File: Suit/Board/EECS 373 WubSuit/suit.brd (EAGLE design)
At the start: 100 x 80 mm, 44 parts, among them U1 ATMEGA328P_PDIP

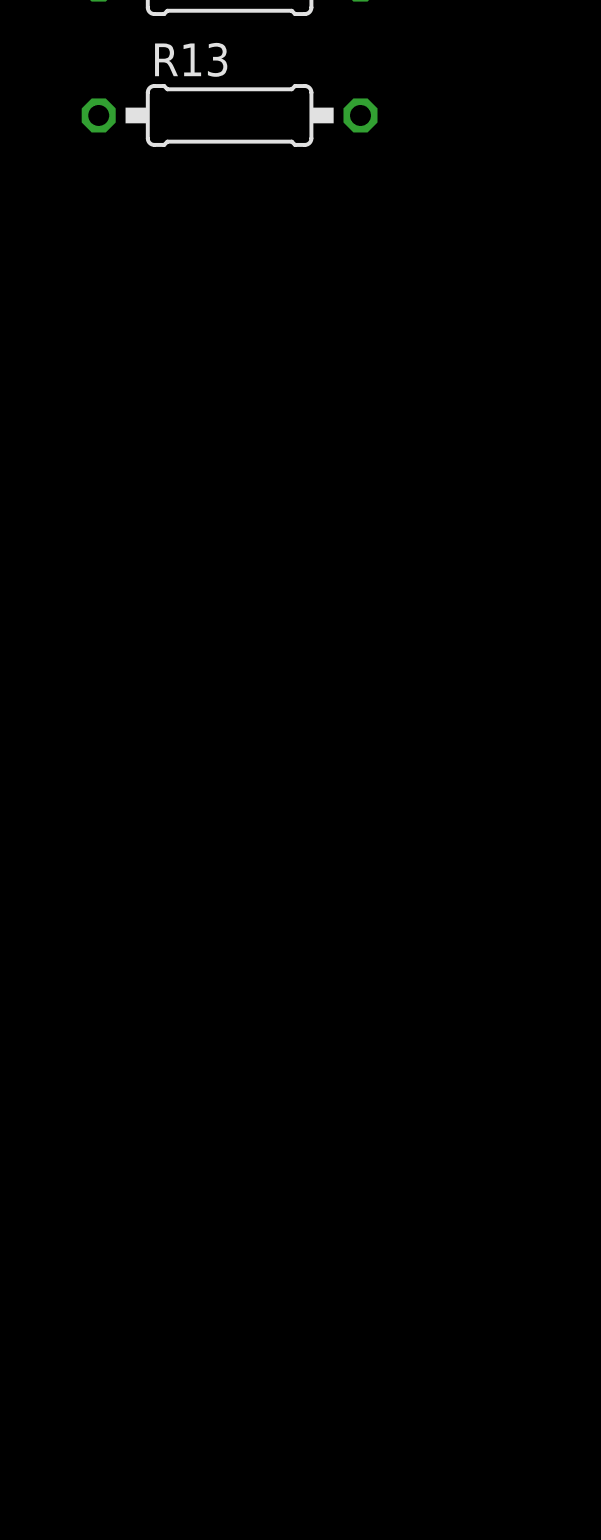
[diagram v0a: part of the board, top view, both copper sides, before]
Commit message: added more board/sch files
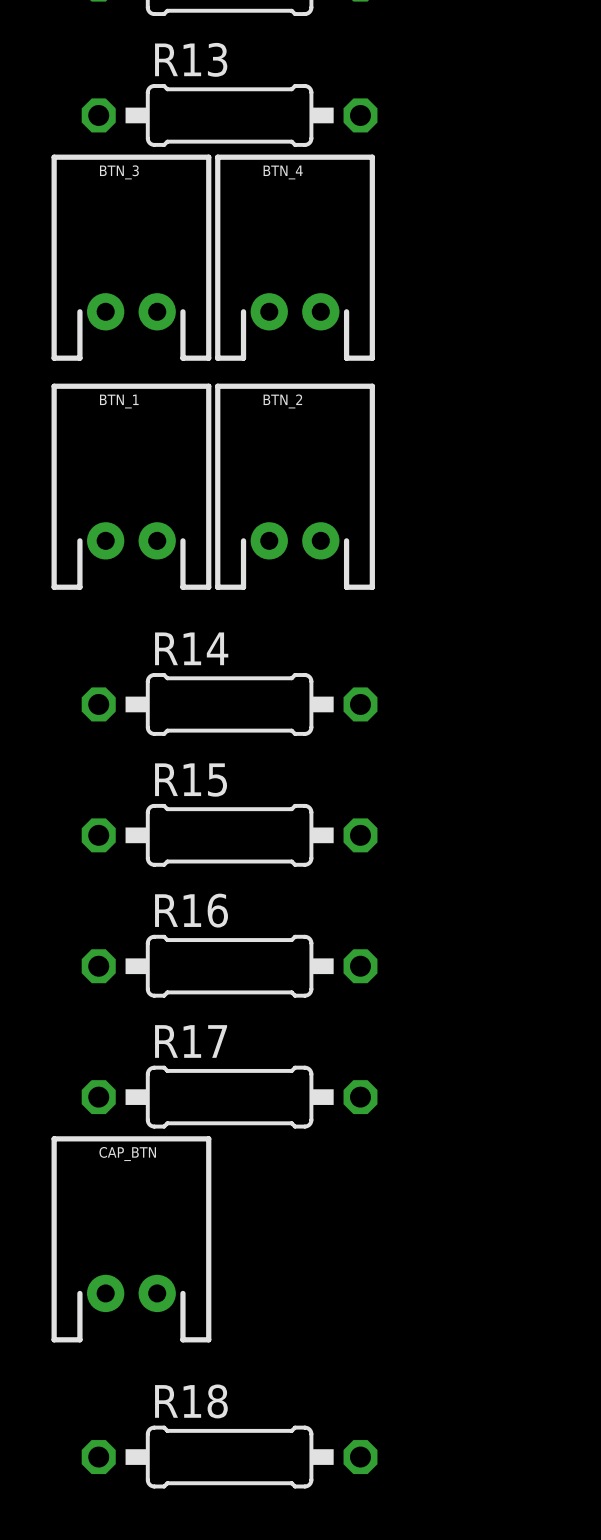
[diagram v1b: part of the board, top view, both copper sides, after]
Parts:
- added BTN_1, BTN_2, BTN_3, BTN_4, CAP_BTN: M02JST-PTH-2, SparkFun-Connectors:JST-2-PTH
- added R14, R15, R16, R17, R18: 10k, resistor:0207/10
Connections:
- new net BTN_1: BTN_1.1, R17.1, XB1.17
- new net BTN_2: BTN_2.1, R16.1, XB1.11
- new net BTN_3: BTN_3.1, R15.1, XB1.15
- new net BTN_4: BTN_4.1, R14.1, XB1.16
- net CAP_BTN: now also CAP_BTN.1, R18.1
- net GND: now also MMA8452.1, R14.2, R15.2, R16.2, R17.2, R18.2
- net RST: now also XB1.5
- net SCL: now also MMA8452.4
- net SDA: now also MMA8452.5
- net VCC: now also BTN_1.2, BTN_2.2, BTN_3.2, BTN_4.2, CAP_BTN.2, MMA8452.6
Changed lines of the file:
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@@
 <element name="R12" library="resistor" package="0207/10" value="1M" x="-152.4" y="-267.97"/>
 <element name="R13" library="resistor" package="0207/10" value="1M" x="-152.4" y="-273.05"/>
+<element name="BTN_1" library="SparkFun-Connectors" package="JST-2-PTH" value="M02JST-PTH-2" x="-156.21" y="-289.56"/>
+<element name="BTN_2" library="SparkFun-Connectors" package="JST-2-PTH" value="M02JST-PTH-2" x="-149.86" y="-289.56"/>
+<element name="BTN_3" library="SparkFun-Connectors" package="JST-2-PTH" value="M02JST-PTH-2" x="-156.21" y="-280.67"/>
+<element name="BTN_4" library="SparkFun-Connectors" package="JST-2-PTH" value="M02JST-PTH-2" x="-149.86" y="-280.67"/>
+<element name="R14" library="resistor" package="0207/10" value="10k" x="-152.4" y="-295.91"/>
+<element name="R15" library="resistor" package="0207/10" value="10k" x="-152.4" y="-300.99"/>
+<element name="R16" library="resistor" package="0207/10" value="10k" x="-152.4" y="-306.07"/>
+<element name="R17" library="resistor" package="0207/10" value="10k" x="-152.4" y="-311.15"/>
+<element name="CAP_BTN" library="SparkFun-Connectors" package="JST-2-PTH" value="M02JST-PTH-2" x="-156.21" y="-318.77"/>
+<element name="R18" library="resistor" package="0207/10" value="10k" x="-152.4" y="-325.12"/>
 </elements>
 <signals>
@@
 <contactref element="R11" pad="2"/>
 <contactref element="R10" pad="2"/>
+<contactref element="BTN_1" pad="2"/>
+<contactref element="BTN_4" pad="2"/>
+<contactref element="BTN_3" pad="2"/>
+<contactref element="BTN_2" pad="2"/>
+<contactref element="MMA8452" pad="6"/>
+<contactref element="CAP_BTN" pad="2"/>
 <wire x1="-140.97" y1="-129.54" x2="-124.46" y2="-114.3" width="0" layer="19" extent="1-1"/>
 <wire x1="-151.13" y1="-142.24" x2="-140.97" y2="-129.54" width="0" layer="19" extent="1-1"/>
@@
 <wire x1="-140.97" y1="-231.14" x2="-148.59" y2="-217.17" width="0" layer="19" extent="1-1"/>
 <wire x1="-140.97" y1="-236.22" x2="-140.97" y2="-231.14" width="0" layer="19" extent="1-1"/>
-<wire x1="-72.39" y1="-64.77" x2="-124.46" y2="-114.3" width="0" layer="19" extent="1-1"/>
+<wire x1="-148.86" y1="-280.67" x2="-140.97" y2="-236.22" width="0" layer="19" extent="1-1"/>
+<wire x1="-155.21" y1="-280.67" x2="-148.86" y2="-280.67" width="0" layer="19" extent="1-1"/>
+<wire x1="-155.21" y1="-289.56" x2="-155.21" y2="-280.67" width="0" layer="19" extent="1-1"/>
+<wire x1="-148.86" y1="-289.56" x2="-155.21" y2="-289.56" width="0" layer="19" extent="1-1"/>
+<wire x1="-155.21" y1="-318.77" x2="-155.21" y2="-289.56" width="0" layer="19" extent="1-1"/>
+<wire x1="-59.69" y1="-105.664" x2="-124.46" y2="-114.3" width="0" layer="19" extent="1-1"/>
+<wire x1="-72.39" y1="-64.77" x2="-59.69" y2="-105.664" width="0" layer="19" extent="1-1"/>
 <wire x1="-33.02" y1="2.54" x2="-72.39" y2="-64.77" width="0" layer="19" extent="1-1"/>
 <wire x1="-30.48" y1="10.16" x2="-33.02" y2="2.54" width="0" layer="19" extent="1-1"/>
@@
 <contactref element="R13" pad="1"/>
 <contactref element="R12" pad="1"/>
+<contactref element="R14" pad="2"/>
+<contactref element="R17" pad="2"/>
+<contactref element="R16" pad="2"/>
+<contactref element="R15" pad="2"/>
+<contactref element="MMA8452" pad="1"/>
+<contactref element="R18" pad="2"/>
 <wire x1="-126.2888" y1="-100.6094" x2="-119.38" y2="-114.3" width="0" layer="19" extent="1-1"/>
 <wire x1="-144.78" y1="-114.3" x2="-126.2888" y2="-100.6094" width="0" layer="19" extent="1-1"/>
@@
 <wire x1="-157.48" y1="-267.97" x2="-155.21" y2="-243.84" width="0" layer="19" extent="1-1"/>
 <wire x1="-157.48" y1="-273.05" x2="-157.48" y2="-267.97" width="0" layer="19" extent="1-1"/>
+<wire x1="-147.32" y1="-295.91" x2="-157.48" y2="-273.05" width="0" layer="19" extent="1-1"/>
+<wire x1="-147.32" y1="-300.99" x2="-147.32" y2="-295.91" width="0" layer="19" extent="1-1"/>
+<wire x1="-147.32" y1="-306.07" x2="-147.32" y2="-300.99" width="0" layer="19" extent="1-1"/>
+<wire x1="-147.32" y1="-311.15" x2="-147.32" y2="-306.07" width="0" layer="19" extent="1-1"/>
+<wire x1="-147.32" y1="-325.12" x2="-147.32" y2="-311.15" width="0" layer="19" extent="1-1"/>
 <wire x1="-76.2" y1="-102.87" x2="-119.38" y2="-114.3" width="0" layer="19" extent="1-1"/>
+<wire x1="-72.39" y1="-105.156" x2="-76.2" y2="-102.87" width="0" layer="19" extent="1-1"/>
 <wire x1="-73.23" y1="6.24" x2="-76.2" y2="-102.87" width="0" layer="19" extent="1-1"/>
 <wire x1="-33.02" y1="10.16" x2="-73.23" y2="6.24" width="0" layer="19" extent="1-1"/>
@@
 <contactref element="S1" pad="4"/>
 <contactref element="R2" pad="1"/>
+<contactref element="XB1" pad="5"/>
 <wire x1="-126.2888" y1="-105.1306" x2="-135.89" y2="-114.3" width="0" layer="19" extent="1-1"/>
 <wire x1="-151.13" y1="-129.54" x2="-135.89" y2="-114.3" width="0" layer="19" extent="1-1"/>
-<wire x1="-48.26" y1="2.54" x2="-126.2888" y2="-105.1306" width="0" layer="19" extent="1-1"/>
+<wire x1="-73.23" y1="16.24" x2="-126.2888" y2="-105.1306" width="0" layer="19" extent="1-1"/>
+<wire x1="-48.26" y1="2.54" x2="-73.23" y2="16.24" width="0" layer="19" extent="1-1"/>
 </signal>
 <signal name="N$5">
@@
 <contactref element="PCF8574N" pad="15"/>
 <contactref element="R10" pad="1"/>
-<wire x1="-146.05" y1="-217.17" x2="-151.13" y2="-231.14" width="0" layer="19" extent="1-1"/>
-<wire x1="-45.72" y1="10.16" x2="-146.05" y2="-217.17" width="0" layer="19" extent="1-1"/>
+<contactref element="MMA8452" pad="5"/>
+<wire x1="-45.72" y1="10.16" x2="-62.23" y2="-105.156" width="0" layer="19" extent="1-1"/>
+<wire x1="-146.05" y1="-217.17" x2="-62.23" y2="-105.156" width="0" layer="19" extent="1-1"/>
+<wire x1="-151.13" y1="-231.14" x2="-146.05" y2="-217.17" width="0" layer="19" extent="1-1"/>
 </signal>
 <signal name="XB_RX">
@@
 </signal>
 <signal name="SCL">
+<contactref element="R11" pad="1"/>
+<contactref element="MMA8452" pad="4"/>
 <contactref element="PCF8574N" pad="14"/>
-<contactref element="R11" pad="1"/>
-<wire x1="-143.51" y1="-217.17" x2="-151.13" y2="-236.22" width="0" layer="19" extent="1-1"/>
+<wire x1="-143.51" y1="-217.17" x2="-64.77" y2="-105.664" width="0" layer="19" extent="1-1"/>
+<wire x1="-151.13" y1="-236.22" x2="-143.51" y2="-217.17" width="0" layer="19" extent="1-1"/>
 </signal>
 <signal name="CAP_BTN">
 <contactref element="XB1" pad="20"/>
+<contactref element="R18" pad="1"/>
+<contactref element="CAP_BTN" pad="1"/>
+<wire x1="-157.21" y1="-318.77" x2="-157.48" y2="-325.12" width="0" layer="19" extent="1-1"/>
+<wire x1="-51.23" y1="24.24" x2="-157.21" y2="-318.77" width="0" layer="19" extent="1-1"/>
 </signal>
 <signal name="PIEZOINT_L">
@@
 <wire x1="-157.21" y1="-252.73" x2="-157.21" y2="-261.62" width="0" layer="19" extent="1-1"/>
 </signal>
+<signal name="BTN_1">
+<contactref element="XB1" pad="17"/>
+<contactref element="BTN_1" pad="1"/>
+<contactref element="R17" pad="1"/>
+<wire x1="-157.21" y1="-289.56" x2="-157.48" y2="-311.15" width="0" layer="19" extent="1-1"/>
+<wire x1="-51.23" y1="18.24" x2="-157.21" y2="-289.56" width="0" layer="19" extent="1-1"/>
+</signal>
+<signal name="BTN_2">
+<contactref element="XB1" pad="11"/>
+<contactref element="R16" pad="1"/>
+<contactref element="BTN_2" pad="1"/>
+<wire x1="-150.86" y1="-289.56" x2="-157.48" y2="-306.07" width="0" layer="19" extent="1-1"/>
+<wire x1="-51.23" y1="6.24" x2="-150.86" y2="-289.56" width="0" layer="19" extent="1-1"/>
+</signal>
+<signal name="BTN_3">
+<contactref element="XB1" pad="15"/>
+<contactref element="R15" pad="1"/>
+<contactref element="BTN_3" pad="1"/>
+<wire x1="-157.21" y1="-280.67" x2="-157.48" y2="-300.99" width="0" layer="19" extent="1-1"/>
+<wire x1="-51.23" y1="14.24" x2="-157.21" y2="-280.67" width="0" layer="19" extent="1-1"/>
+</signal>
+<signal name="BTN_4">
+<contactref element="XB1" pad="16"/>
+<contactref element="BTN_4" pad="1"/>
+<contactref element="R14" pad="1"/>
+<wire x1="-150.86" y1="-280.67" x2="-157.48" y2="-295.91" width="0" layer="19" extent="1-1"/>
+<wire x1="-51.23" y1="16.24" x2="-150.86" y2="-280.67" width="0" layer="19" extent="1-1"/>
+</signal>
 </signals>

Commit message: working on board layout and routing
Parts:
- removed LED1, LED2, LED3, LED4, LED5, LED6, LED7, LED8: (no value), led:LED5MM
- moved CAP_BTN 468.6 mm to (94.0, 77.5)
- moved R18 463.8 mm to (92.7, 68.6), turned to 270 degrees
- moved R17 448.6 mm to (86.4, 68.6), turned to 270 degrees
- moved R16 440.9 mm to (80.0, 68.6), turned to 270 degrees
- moved BTN_1 440.6 mm to (87.6, 77.5)
- moved BTN_2 433.7 mm to (81.3, 77.5)
- moved R15 433.2 mm to (73.7, 68.6), turned to 270 degrees
- moved BTN_3 426.3 mm to (74.9, 77.5)
- moved R14 425.6 mm to (67.3, 68.6), turned to 270 degrees
- moved BTN_4 419.5 mm to (68.6, 77.5)
- moved R13 376.6 mm to (8.89, 67.3), turned to 90 degrees
- moved R12 371.0 mm to (6.35, 67.3), turned to 90 degrees
- moved FLEX_R 352.7 mm to (2.54, 53.3), turned to 90 degrees
- moved FLEX_L 350.4 mm to (2.54, 59.7), turned to 90 degrees
- moved PIEZO_R 348.2 mm to (2.54, 66.0), turned to 90 degrees
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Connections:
- removed net N$10: LED6.A, R7.2
- removed net N$11: LED7.A, R8.2
- removed net N$12: LED8.A, R9.2
- removed net N$2: LED1.A, R1.2
- removed net N$3: LED2.A, R3.2
- net LED_0: now also R1.1; no longer LED1.K
- net LED_1: now also R3.1; no longer LED2.K
- net LED_2: now also R4.1; no longer LED3.K
- net LED_3: no longer C7.1, LED4.K
- net LED_4: no longer C8.1, LED5.K
- net LED_5: no longer C9.1, LED6.K
- net LED_6: now also R8.1; no longer LED7.K
- net LED_7: now also R9.1; no longer LED8.K
- net N$7: now also C7.1, R5.1; no longer LED3.A, R4.2
- net N$8: now also C8.1, R6.1; no longer LED4.A, R5.2
- net N$9: now also C9.1, R7.1; no longer LED5.A, R6.2
- net VCC: now also R1.2, R4.2, R5.2, R6.2, R7.2, R8.2, R9.2; no longer R1.1, R3.1, R4.1, R5.1, R6.1, R7.1, R8.1, R9.1
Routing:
- net GND: track 0.00 -> 214.3 mm
- net VCC: track 0.00 -> 196.9 mm
- net LED_5: track 0.00 -> 87.3 mm
- net RST: track 0.00 -> 67.4 mm
- net LED_0: track 0.00 -> 66.3 mm
- net PIEZO_L: track 0.00 -> 59.7 mm
- net PIEZOINT_R: track 0.00 -> 58.0 mm
- net BTN_4: track 0.00 -> 57.0 mm
- net BTN_2: track 0.00 -> 56.9 mm
- net PIEZO_R: track 0.00 -> 53.0 mm
- net SDA: track 0.00 -> 49.5 mm, vias 0 -> 1
- net LED_7: track 0.00 -> 48.0 mm, vias 0 -> 1
- net LED_1: track 0.00 -> 45.0 mm
- net BTN_3: track 0.00 -> 41.7 mm
- net SCL: track 0.00 -> 40.9 mm
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- added copper zone on layer 16, net GND
- added copper zone on layer 1, net VCC

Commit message: almost done with the board layout and routing, need to add power headers
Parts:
- removed JP2: FTDI_BASICPTH, SparkFun-Connectors:FTDI_BASIC
- removed LED_OUT: (no value), SparkFun-Connectors:1X08_LOCK
- removed MMA8452: (no value), SparkFun-Connectors:1X06_FEMALE_LOCK.010
- removed U1: ATMEGA328P_PDIP, SparkFun-DigitalIC:DIL28-3
- removed XB1: XBEE, maxstream:XBEE
- added $1_39_$: ATMEGA328P_PDIP, SparkFun-DigitalIC:DIL28-3
- added $1_40_$: XBEE, maxstream:XBEE
- added JP1: FTDI_BASICPTH, SparkFun-Connectors:FTDI_BASIC
- added LED_01, LED_23, LED_45, LED_67: M02JST-PTH-2, SparkFun-Connectors:JST-2-PTH
- added MMA1: (no value), SparkFun-Connectors:1X06_FEMALE_LOCK.010
- added R19, R20: 10k, resistor:0207/10
- R11: value (none) -> 10k
- R12, R13: value 1M -> (none)
- R14: value 10k -> (none)
- R15, R16: value 10k -> 1M
- moved R16 72.6 mm to (7.62, 73.7), turned to 0 degrees
- moved R7 68.2 mm to (27.9, 8.89), turned to 270 degrees
- moved R6 64.9 mm to (30.5, 8.89), turned to 270 degrees
- moved CAP_BTN 58.4 mm to (35.6, 77.5)
- moved R4 58.3 mm to (35.6, 8.89), turned to 270 degrees
- moved R12 57.7 mm to (50.8, 30.5), turned to 0 degrees
- moved PCF8574N 57.1 mm to (49.5, 14.0)
- moved R5 56.9 mm to (33.0, 8.89), turned to 270 degrees
- moved R10 56.1 mm to (50.8, 27.9), turned to 0 degrees
- moved R1 55.7 mm to (24.1, 12.7), turned to 90 degrees
- moved R15 53.3 mm to (20.3, 68.6), turned to 90 degrees
- moved R9 51.1 mm to (50.8, 25.4)
- moved R8 51.1 mm to (50.8, 22.9)
- moved S1 49.6 mm to (11.4, 41.9), turned to 180 degrees
- moved C9 48.6 mm to (61.0, 25.4), turned to 180 degrees
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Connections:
- removed net N$13: FLEX_L.1, FLEX_R.1
- new net N$2: FLEX_R.1, R14.2
- net BTN_1: now also $1_40_$.17; no longer XB1.17
- net BTN_2: now also $1_40_$.11, R18.1; no longer R16.1, XB1.11
- net BTN_3: now also $1_40_$.15, R19.1; no longer R15.1, XB1.15
- net BTN_4: now also $1_40_$.16, R20.1; no longer R14.1, XB1.16
- net CAP_BTN: now also $1_40_$.20, R11.1; no longer R18.1, XB1.20
- net FLEX_L: now also $1_39_$.25, FLEX_L.2; no longer U1.25
- net FLEX_R: now also $1_39_$.26, FLEX_R.2; no longer U1.26
- net FTDI_RX: now also $1_39_$.3, JP1.RXI; no longer JP2.RXI, U1.3
- net FTDI_TX: now also $1_39_$.2, JP1.TXO; no longer JP2.TXO, U1.2
- net GND: now also $1_39_$.22, $1_39_$.8, $1_40_$.10, C2.1, C4.2, JP1.GND, MMA1.1, R11.2, R15.1, R16.1, R19.2, R20.2; no longer C1.2, C4.1, JP2.GND, MMA8452.1, R12.1, R13.1, R14.2, R15.2, R16.2, U1.22, U1.8, XB1.10
- net LED_0: now also C4.1, LED_01.2, R4.1; no longer C1.1, LED_OUT.1, R1.1
- net LED_1: now also LED_01.1, R5.1; no longer LED_OUT.2, R3.1
- net LED_2: now also LED_23.2, R6.1; no longer LED_OUT.3, R4.1
- net LED_3: now also LED_23.1; no longer LED_OUT.4
- net LED_4: now also LED_45.2; no longer LED_OUT.5
- net LED_5: now also LED_45.1; no longer LED_OUT.6
- net LED_6: now also LED_67.2, R10.1; no longer LED_OUT.7, R8.1
- net LED_7: now also LED_67.1, R12.1; no longer LED_OUT.8, R9.1
- net N$1: now also FLEX_L.1, R13.2; no longer FLEX_L.2, FLEX_R.2
- net N$4: now also C1.1, JP1.DTR; no longer C2.1, JP2.DTR
- net N$5: now also $1_39_$.10; no longer U1.10
- net N$6: now also $1_39_$.9, C2.2; no longer C4.2, U1.9
- net N$7: now also R7.1; no longer R5.1
- net N$8: now also R8.1; no longer R6.1
- net N$9: now also R9.1; no longer R7.1
- net PIEZOINT_L: now also $1_39_$.4, $1_40_$.19; no longer U1.4, XB1.19
- net PIEZOINT_R: now also $1_39_$.5, $1_40_$.18; no longer U1.5, XB1.18
- net PIEZO_L: now also $1_39_$.23, R15.2; no longer R12.2, U1.23
- net PIEZO_R: now also $1_39_$.24, R16.2; no longer R13.2, U1.24
- net RST: now also $1_39_$.1, $1_40_$.5, C1.2, R3.1; no longer C2.2, R2.1, U1.1, XB1.5
- net SCL: now also MMA1.4, R2.1; no longer MMA8452.4, R11.1
- net SDA: now also $1_39_$.27, MMA1.5, R1.1; no longer MMA8452.5, R10.1, U1.27
- net VCC: now also $1_39_$.20, $1_39_$.21, $1_39_$.7, $1_40_$.1, $1_40_$.14, JP1.VCC, MMA1.6, R12.2, R13.1, R14.1, R3.2; no longer JP2.VCC, MMA8452.6, R11.2, U1.20, U1.21, U1.7, XB1.1, XB1.14
- net XB_RX: now also $1_39_$.17, $1_40_$.3; no longer U1.17, XB1.3
- net XB_TX: now also $1_39_$.16, $1_40_$.2; no longer U1.16, XB1.2
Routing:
- net VCC: track 196.9 -> 4.60 mm
- net GND: track 214.3 -> 26.5 mm, vias 0 -> 2
- net LED_5: track 87.3 -> 19.9 mm
- net SDA: track 49.5 -> 99.8 mm, vias 1 -> 0
- net PIEZOINT_L: track 0.00 -> 43.1 mm, vias 0 -> 1
- net LED_0: track 66.3 -> 35.2 mm
- net FLEX_L: track 0.00 -> 30.3 mm
- net FLEX_R: track 0.00 -> 28.8 mm
- net XB_RX: track 14.2 -> 43.0 mm
- net XB_TX: track 0.00 -> 27.8 mm
- net N$9: track 7.40 -> 33.0 mm
- net FTDI_RX: track 8.15 -> 32.8 mm, vias 0 -> 1
- net N$5: track 9.42 -> 32.3 mm
- net N$6: track 9.42 -> 32.1 mm
- net LED_6: track 34.3 -> 56.4 mm
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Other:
- board size 100 x 80 mm -> 67.1 x 80.1 mm
- board text added: "1 0"
- board text added: "3 2"
- board text added: "5 4"
- board text added: "7 6"
- board text added: "LED HEADERS"
- board text added: "Wubsuit EECS373 FA 2013 University of Michigan"

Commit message: finished and ordered board
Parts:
- added C12, C13: 220uF, rcl:B45181A
- added IC1: (no value), linear:TO92
- added VIN: M02JST-PTH-2, SparkFun-Connectors:JST-2-PTH
- added X1: MINI-USB_4P-85-32004-10X, con-cypressindustries:85-32004-10X
- moved Q1 10.6 mm to (15.4, 27.8), turned to 180 degrees
- moved C2 8.94 mm to (16.2, 35.3), turned to 0 degrees
- moved C3 8.15 mm to (16.2, 32.1), turned to 0 degrees
- moved LED_01 3.84 mm to (42.7, 6.30)
- moved LED_23 3.84 mm to (49.0, 6.30)
- moved LED_45 3.84 mm to (55.4, 6.30)
- moved LED_67 3.84 mm to (61.7, 6.30)
- moved R17 3.27 mm to (59.7, 70.6)
- moved BTN_1 2.22 mm to (61.7, 79.6)
- moved BTN_2 2.22 mm to (55.4, 79.6)
- moved BTN_3 2.22 mm to (49.0, 79.6)
- moved BTN_4 2.22 mm to (42.7, 79.6)
- moved CAP_BTN 2.22 mm to (36.3, 79.6)
- moved FLEX_L 2.22 mm to (30.0, 79.6)
- moved FLEX_R 2.22 mm to (23.6, 79.6)
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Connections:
- new net N$10: IC1.2, VIN.1, X1.1
- net GND: now also C12.-, C13.-, IC1.1, VIN.2, X1.4
- net SCL: now also $1_39_$.28
- net VCC: now also C12.+, C13.+, IC1.3
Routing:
- net SCL: track 51.4 -> 98.1 mm, vias 0 -> 3
- net N$10: track 0.00 -> 22.0 mm
- net N$5: track 32.3 -> 13.3 mm
- net N$6: track 32.1 -> 20.1 mm
- net GND: track 26.5 -> 22.7 mm, vias 2 -> 12
- net BTN_1: track 35.4 -> 32.6 mm
- net LED_0: track 35.2 -> 32.4 mm
- net LED_2: track 55.4 -> 52.8 mm
- net LED_5: track 19.9 -> 18.2 mm
- net LED_4: track 30.1 -> 28.4 mm
- net LED_6: track 56.4 -> 54.7 mm
- net LED_7: track 68.6 -> 66.9 mm
- net LED_1: track 44.1 -> 43.0 mm
- net LED_3: track 11.0 -> 9.90 mm
- added copper zone on layer 1, net GND
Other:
- board size 67.1 x 80.1 mm -> 66.4 x 86.1 mm
- board text added: "+"
- board text added: "-"
- board text added: "Brian Margosian"
- board text added: "WubSuit EECS 373 FA 2013"
- board text removed: "LED HEADERS"
- board text removed: "Wubsuit EECS373 FA 2013 University of Michigan"
